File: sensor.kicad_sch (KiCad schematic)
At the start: 1 part, among them U3 BNO055

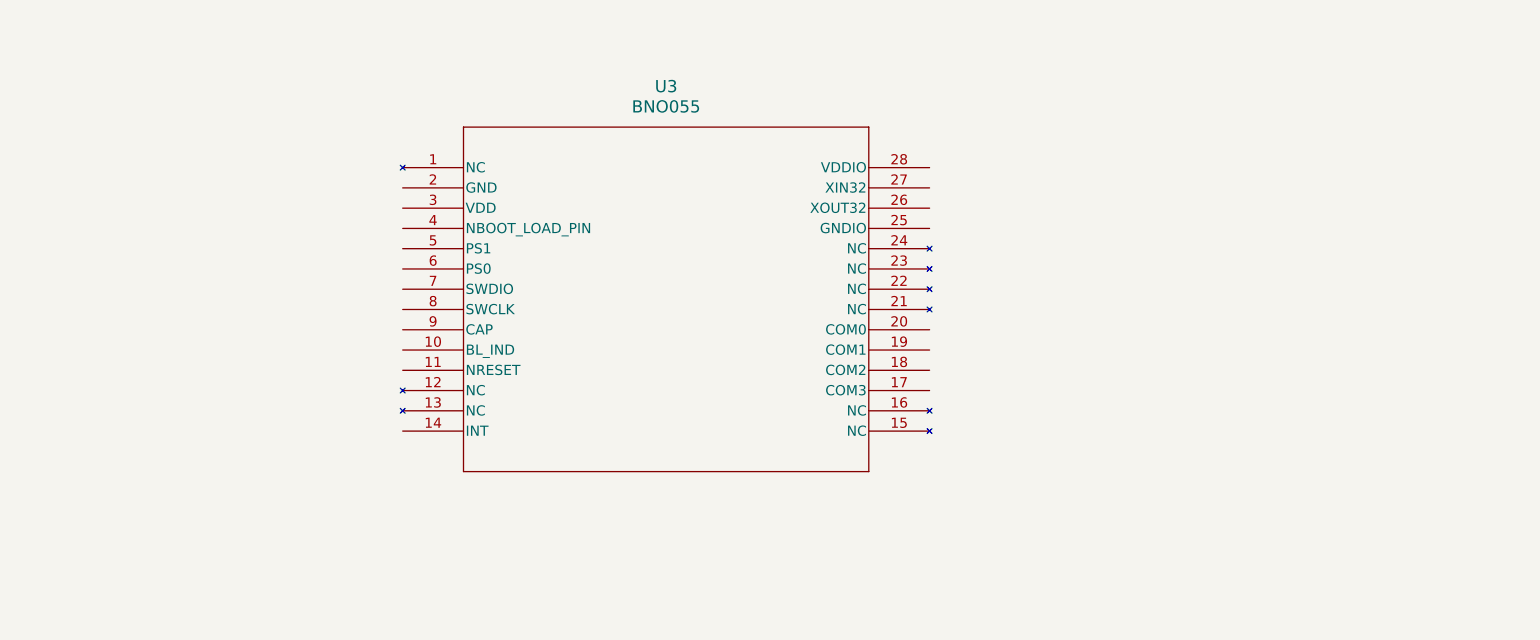
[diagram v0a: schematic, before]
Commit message: wiring the IMU as per its datasheet app circuit. started with power rails
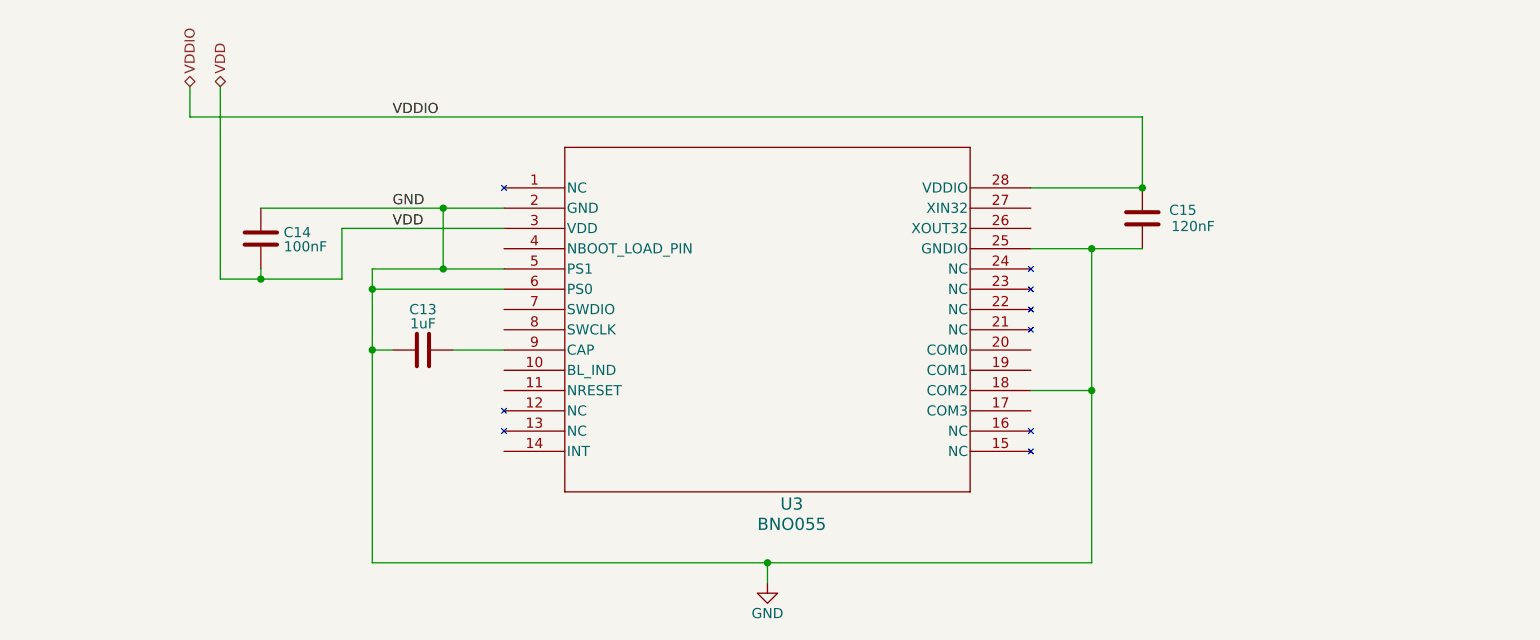
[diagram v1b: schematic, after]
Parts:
- added C13: 1uF, symbol Device:C
- added C14: 100nF, symbol Device:C
- added C15: 120nF, symbol Device:C
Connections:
- net GND: now reaches U3.18 (COM2)
- net GND: now also U3.2 (GND), U3.25 (GNDIO), U3.5 (PS1), U3.6 (PS0), C13.1, C14.1, C15.2
- net VDDIO: now reaches U3.28 (VDDIO)
- net VDDIO: now also C15.1
- net VDD: now reaches U3.3 (VDD)
- net VDD: now also C14.2
- net at U3.9 (CAP): now also C13.2
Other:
- moved on the sheet: U3

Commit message: i2c wiring for imu
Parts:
- added R7: 10k, symbol Device:R
- added R8, R9: 4.7k, symbol Device:R
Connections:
- net VDDIO: now also R7.1, R8.1, R9.1
- net NRST: now reaches U3.11 (NRESET)
- net NRST: now also R7.2
- net I2C_ADDR_SEL: now reaches U3.17 (COM3)
- net SCL : now reaches U3.19 (COM1)
- net SCL : now also R9.2
- net SDA: now reaches U3.20 (COM0)
- net SDA: now also R8.2

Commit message: IMU wiring
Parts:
- added R10: 10k, symbol Device:R
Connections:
- net VDDIO: now also R10.1
- net BL_IND: now reaches U3.10 (BL_IND)
- net INT: now reaches U3.14 (INT)
- net NBOOT_LOAD: now reaches U3.4 (NBOOT_LOAD_PIN)
- net NBOOT_LOAD: now also R10.2
- no-connect marks 0 -> 4
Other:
- moved on the sheet: C14, R7

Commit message: update README. update imu to select address, add notte
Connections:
- net I2C_ADDR_SEL is gone; now on net GND: U3.17 (COM3)
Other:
- note added: "COM3 tied to GND I2C Address = 0x28 BNO055 Data sheet Page 100"
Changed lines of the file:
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@@
 	(generator_version "10.0")
 	(paper "A4")
+	(text "COM3 tied to GND\nI2C Address = 0x28\nBNO055 Data sheet Page 100"
+		(exclude_from_sim no)
+		(at 204.724 103.378 0)
+		(effects
+			(font
+				(size 1.27 1.27)
+			)
+		)
+	)
 	(junction
 		(at 67.31 96.52)
@@
 	(junction
 		(at 186.69 71.12)
+		(diameter 0)
+		(color 0 0 0 0)
+	)
+	(junction
+		(at 186.69 99.06)
 		(diameter 0)
 		(color 0 0 0 0)
@@
 	(wire
 		(pts
+			(xy 172.72 99.06) (xy 186.69 99.06)
+		)
+		(stroke
+			(width 0)
+			(type default)
+		)
+	)
+	(wire
+		(pts
 			(xy 186.69 62.23) (xy 186.69 71.12)
 		)
@@
 	(wire
 		(pts
-			(xy 172.72 99.06) (xy 217.17 99.06)
-		)
-		(stroke
-			(width 0)
-			(type default)
-		)
-	)
-	(wire
-		(pts
 			(xy 60.96 104.14) (xy 106.68 104.14)
 		)
@@
 	(wire
 		(pts
-			(xy 186.69 96.52) (xy 186.69 118.11)
+			(xy 186.69 96.52) (xy 186.69 99.06)
 		)
 		(stroke
@@
 		(pts
 			(xy 106.68 96.52) (xy 67.31 96.52)
+		)
+		(stroke
+			(width 0)
+			(type default)
+		)
+	)
+	(wire
+		(pts
+			(xy 186.69 99.06) (xy 186.69 118.11)
 		)
 		(stroke
@@
 		(effects
 			(font
-				(size 1.27 1.27)
-			)
-			(justify left)
-		)
-	)
-	(hierarchical_label "I2C_ADDR_SEL"
-		(shape bidirectional)
-		(at 217.17 99.06 0)
-		(effects
-			(font
